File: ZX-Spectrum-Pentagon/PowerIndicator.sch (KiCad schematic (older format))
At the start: 6 parts

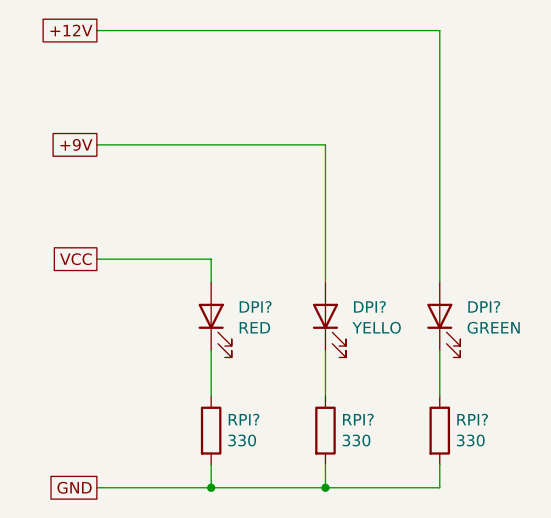
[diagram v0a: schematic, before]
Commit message: move from globag label to hierarchical label. fix all warning
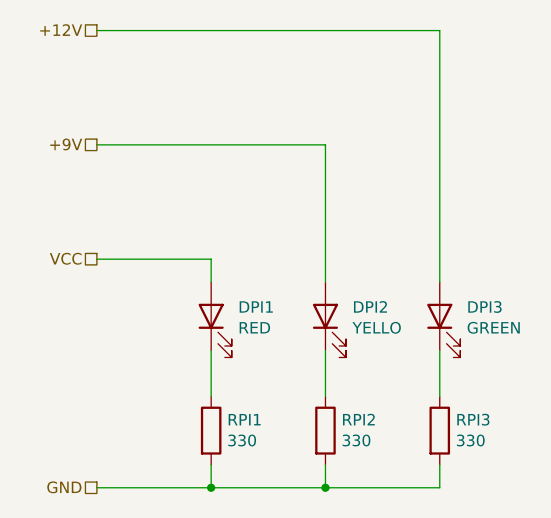
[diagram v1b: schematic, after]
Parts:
- gave numbers to parts that had none: 6
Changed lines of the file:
@@
 Comment4 ""
 $EndDescr
-Text GLabel 1000 1000 0    50   UnSpc ~ 0
+Text HLabel 1000 1000 0    50   UnSpc ~ 0
 +12V
-Text GLabel 1000 1500 0    50   UnSpc ~ 0
+Text HLabel 1000 1500 0    50   UnSpc ~ 0
 +9V
-Text GLabel 1000 2000 0    50   UnSpc ~ 0
+Text HLabel 1000 2000 0    50   UnSpc ~ 0
 VCC
-Text GLabel 1000 3000 0    50   UnSpc ~ 0
+Text HLabel 1000 3000 0    50   UnSpc ~ 0
 GND
 $Comp
-L Device:R RPI?
+L Device:R RPI1
 U 1 1 66542FB1
 P 1500 2750
-F 0 "RPI?" H 1570 2796 50  0000 L CNN
+F 0 "RPI1" H 1570 2796 50  0000 L CNN
 F 1 "330" H 1570 2705 50  0000 L CNN
 F 2 "Resistor_SMD:R_0805_2012Metric_Pad1.20x1.40mm_HandSolder" V 1430 2750 50  0001 C CNN
@@
 	1500 3000 2000 3000
 $Comp
-L Device:R RPI?
+L Device:R RPI2
 U 1 1 665453C8
 P 2000 2750
-F 0 "RPI?" H 2070 2796 50  0000 L CNN
+F 0 "RPI2" H 2070 2796 50  0000 L CNN
 F 1 "330" H 2070 2705 50  0000 L CNN
 F 2 "Resistor_SMD:R_0805_2012Metric_Pad1.20x1.40mm_HandSolder" V 1930 2750 50  0001 C CNN
@@
 $EndComp
 $Comp
-L Device:R RPI?
+L Device:R RPI3
 U 1 1 6654587A
 P 2500 2750
-F 0 "RPI?" H 2570 2796 50  0000 L CNN
+F 0 "RPI3" H 2570 2796 50  0000 L CNN
 F 1 "330" H 2570 2705 50  0000 L CNN
 F 2 "Resistor_SMD:R_0805_2012Metric_Pad1.20x1.40mm_HandSolder" V 2430 2750 50  0001 C CNN
@@
 $EndComp
 $Comp
-L Device:LED DPI?
+L Device:LED DPI1
 U 1 1 6654603C
 P 1500 2250
-F 0 "DPI?" V 1539 2132 50  0000 R CNN
+F 0 "DPI1" V 1539 2132 50  0000 R CNN
 F 1 "RED" V 1448 2132 50  0000 R CNN
 F 2 "LED_SMD:LED_0805_2012Metric_Pad1.15x1.40mm_HandSolder" H 1500 2250 50  0001 C CNN
@@
 $EndComp
 $Comp
-L Device:LED DPI?
+L Device:LED DPI2
 U 1 1 66547531
 P 2000 2250
-F 0 "DPI?" V 2039 2132 50  0000 R CNN
+F 0 "DPI2" V 2039 2132 50  0000 R CNN
 F 1 "YELLO" V 1948 2132 50  0000 R CNN
 F 2 "LED_SMD:LED_0805_2012Metric_Pad1.15x1.40mm_HandSolder" H 2000 2250 50  0001 C CNN
@@
 $EndComp
 $Comp
-L Device:LED DPI?
+L Device:LED DPI3
 U 1 1 6654811E
 P 2500 2250
-F 0 "DPI?" V 2539 2132 50  0000 R CNN
+F 0 "DPI3" V 2539 2132 50  0000 R CNN
 F 1 "GREEN" V 2448 2132 50  0000 R CNN
 F 2 "LED_SMD:LED_0805_2012Metric_Pad1.15x1.40mm_HandSolder" H 2500 2250 50  0001 C CNN

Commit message: clear annotation
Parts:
- renumbered DPI1 to DPI?, DPI2 to DPI?, DPI3 to DPI?, RPI1 to RPI?, RPI2 to RPI?, RPI3 to RPI?
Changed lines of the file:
@@
 GND
 $Comp
-L Device:R RPI1
+L Device:R RPI?
 U 1 1 66542FB1
 P 1500 2750
-F 0 "RPI1" H 1570 2796 50  0000 L CNN
+F 0 "RPI?" H 1570 2796 50  0000 L CNN
 F 1 "330" H 1570 2705 50  0000 L CNN
 F 2 "Resistor_SMD:R_0805_2012Metric_Pad1.20x1.40mm_HandSolder" V 1430 2750 50  0001 C CNN
@@
 	1500 3000 2000 3000
 $Comp
-L Device:R RPI2
+L Device:R RPI?
 U 1 1 665453C8
 P 2000 2750
-F 0 "RPI2" H 2070 2796 50  0000 L CNN
+F 0 "RPI?" H 2070 2796 50  0000 L CNN
 F 1 "330" H 2070 2705 50  0000 L CNN
 F 2 "Resistor_SMD:R_0805_2012Metric_Pad1.20x1.40mm_HandSolder" V 1930 2750 50  0001 C CNN
@@
 $EndComp
 $Comp
-L Device:R RPI3
+L Device:R RPI?
 U 1 1 6654587A
 P 2500 2750
-F 0 "RPI3" H 2570 2796 50  0000 L CNN
+F 0 "RPI?" H 2570 2796 50  0000 L CNN
 F 1 "330" H 2570 2705 50  0000 L CNN
 F 2 "Resistor_SMD:R_0805_2012Metric_Pad1.20x1.40mm_HandSolder" V 2430 2750 50  0001 C CNN
@@
 $EndComp
 $Comp
-L Device:LED DPI1
+L Device:LED DPI?
 U 1 1 6654603C
 P 1500 2250
-F 0 "DPI1" V 1539 2132 50  0000 R CNN
+F 0 "DPI?" V 1539 2132 50  0000 R CNN
 F 1 "RED" V 1448 2132 50  0000 R CNN
 F 2 "LED_SMD:LED_0805_2012Metric_Pad1.15x1.40mm_HandSolder" H 1500 2250 50  0001 C CNN
@@
 $EndComp
 $Comp
-L Device:LED DPI2
+L Device:LED DPI?
 U 1 1 66547531
 P 2000 2250
-F 0 "DPI2" V 2039 2132 50  0000 R CNN
+F 0 "DPI?" V 2039 2132 50  0000 R CNN
 F 1 "YELLO" V 1948 2132 50  0000 R CNN
 F 2 "LED_SMD:LED_0805_2012Metric_Pad1.15x1.40mm_HandSolder" H 2000 2250 50  0001 C CNN
@@
 $EndComp
 $Comp
-L Device:LED DPI3
+L Device:LED DPI?
 U 1 1 6654811E
 P 2500 2250
-F 0 "DPI3" V 2539 2132 50  0000 R CNN
+F 0 "DPI?" V 2539 2132 50  0000 R CNN
 F 1 "GREEN" V 2448 2132 50  0000 R CNN
 F 2 "LED_SMD:LED_0805_2012Metric_Pad1.15x1.40mm_HandSolder" H 2500 2250 50  0001 C CNN
